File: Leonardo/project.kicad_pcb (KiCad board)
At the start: 2 copper layers, 68.6 x 53.3 mm, 40 parts, among them J3 Barrel_Jack, Q1 PMOS, SW1 RESET, U1 LP2985-3.3, U2 LMV358, U3 NCP1117-1.5, U4 ATMEGA32U4-AU, X1 USB_OTG, Y1 16 Mhz

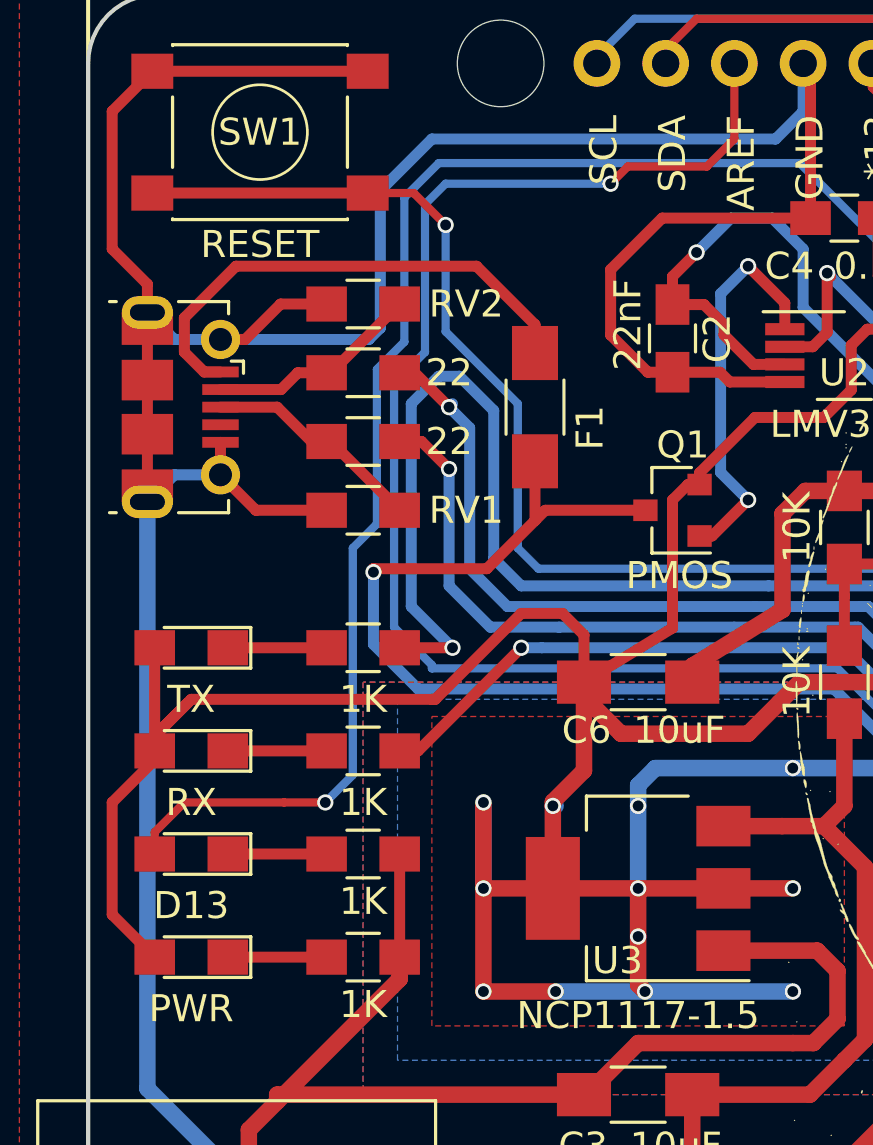
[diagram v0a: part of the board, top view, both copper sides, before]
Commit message: Minor footprint tweaks
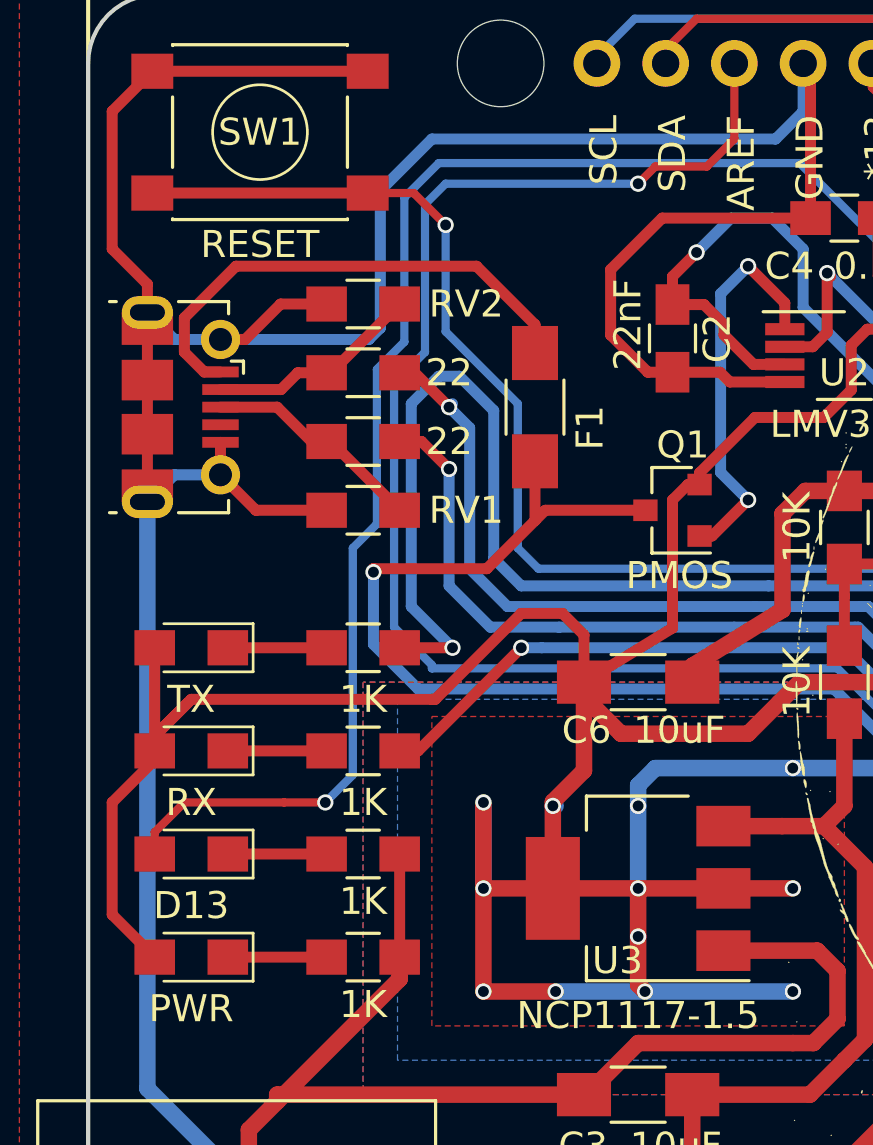
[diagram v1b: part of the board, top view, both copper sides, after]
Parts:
- D1, D3, D4: footprint LEDs:LED_0805_HandSoldering -> footprints:LED_0805_HandSoldering
- D2: footprint LEDs:LED_0805_HandSoldering -> LED_0805_HandSoldering
